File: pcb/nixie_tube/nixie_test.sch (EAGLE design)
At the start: 17 parts, among them IC1 74141N

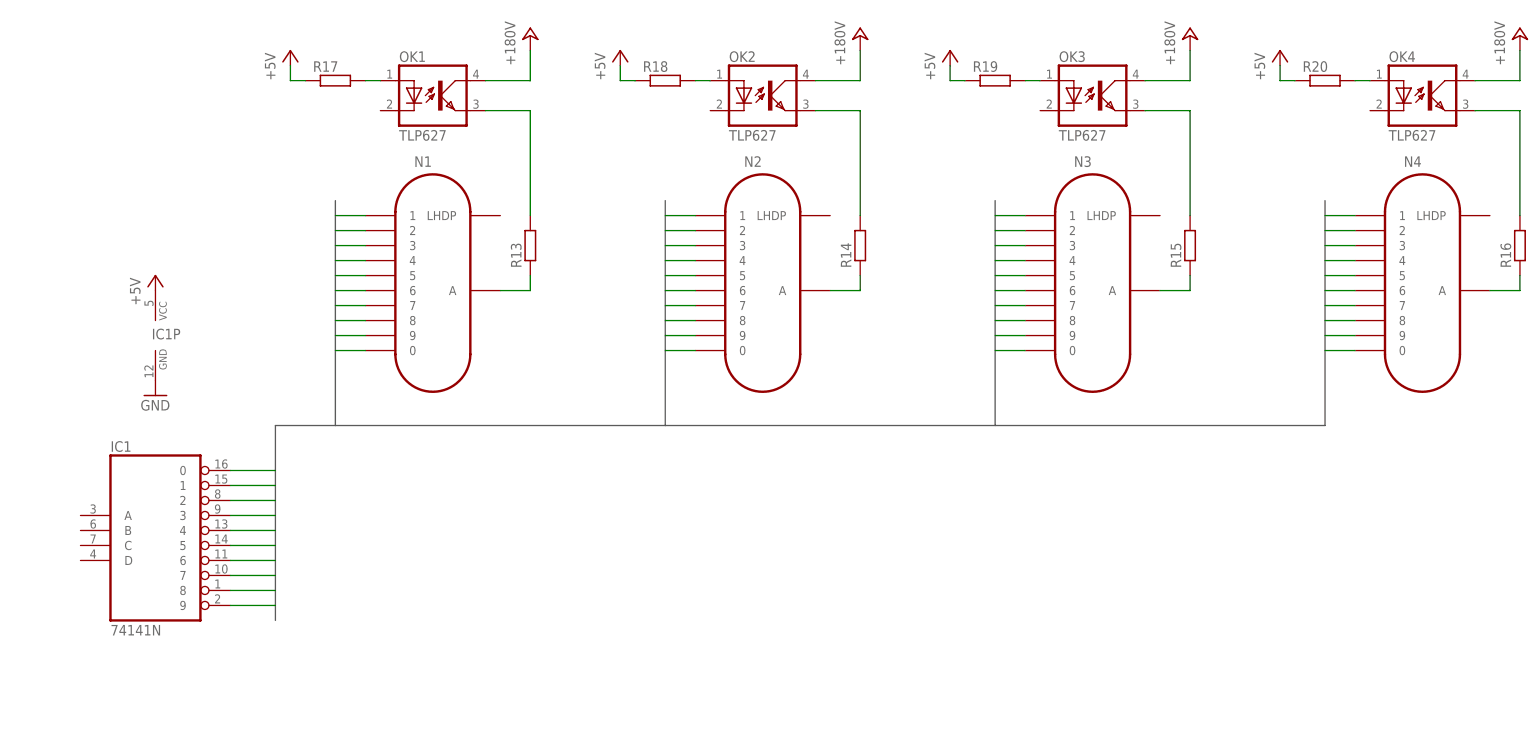
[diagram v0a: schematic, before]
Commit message: 
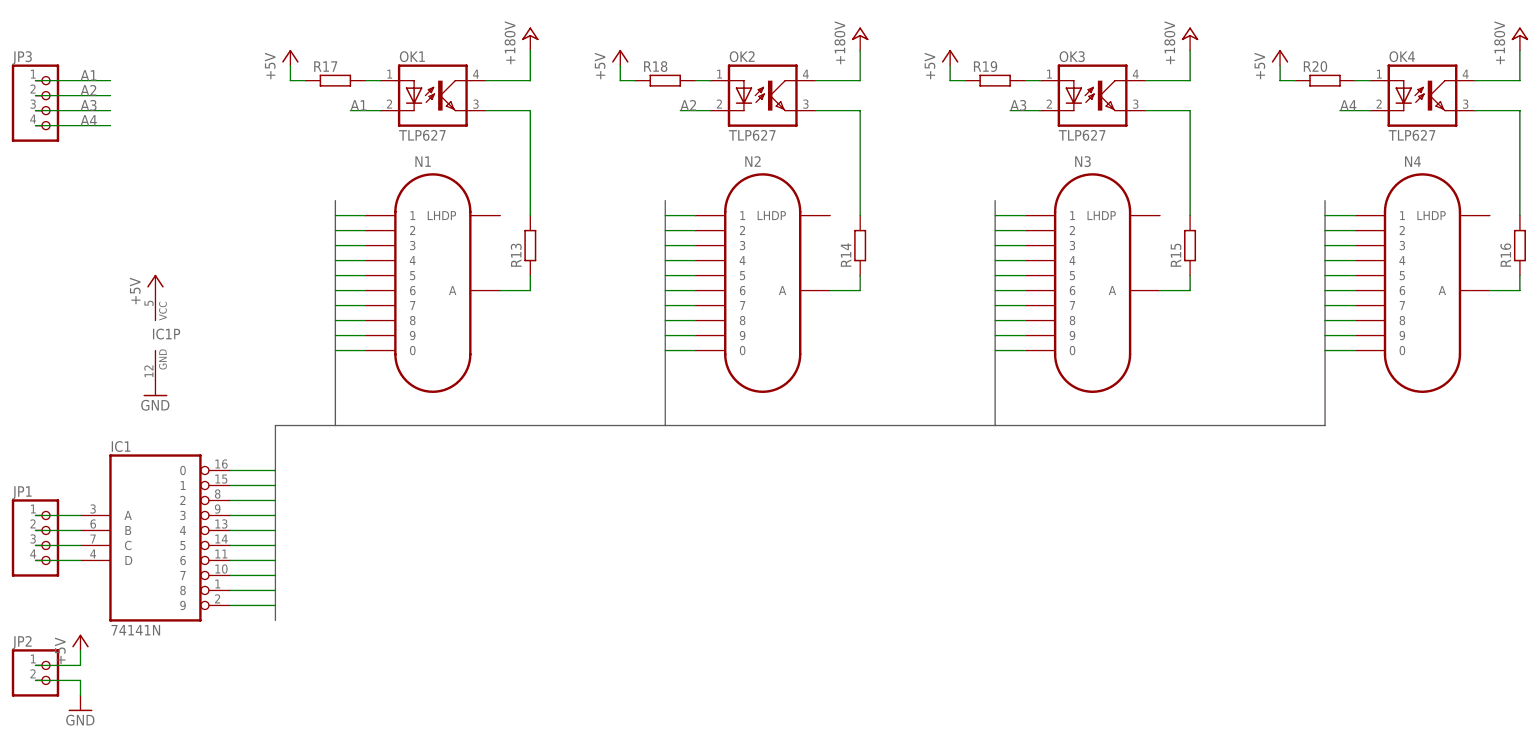
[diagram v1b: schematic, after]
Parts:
- added JP1, JP3: (no value), nixie_tube:PINHD-1X4
- added JP2: (no value), nixie_tube:PINHD-1X2
- R17, R18, R19, R20: device nixie_tube:R-EU_R0805 -> nixie_tube:R-EU_10
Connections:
- new net A1: JP3.1, OK1.C
- new net A2: JP3.2, OK2.C
- new net A3: JP3.3, OK3.C
- new net A4: JP3.4, OK4.C
- new net N$1: IC1A.A, JP1.1
- new net N$2: IC1A.B, JP1.2
- new net N$3: IC1A.C, JP1.3
- new net N$4: IC1A.D, JP1.4
- net +5V: now also JP2.1
- net GND: now also JP2.2
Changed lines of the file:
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@@
 <part name="P+3" library="nixie_tube" deviceset="+180V" device=""/>
 <part name="P+4" library="nixie_tube" deviceset="+180V" device=""/>
-<part name="R17" library="nixie_tube" deviceset="R-EU_" device="R0805"/>
+<part name="R17" library="nixie_tube" deviceset="R-EU_" device="10"/>
 <part name="P+5" library="nixie_tube" deviceset="+5V" device=""/>
-<part name="R18" library="nixie_tube" deviceset="R-EU_" device="R0805"/>
+<part name="R18" library="nixie_tube" deviceset="R-EU_" device="10"/>
 <part name="P+6" library="nixie_tube" deviceset="+5V" device=""/>
-<part name="R19" library="nixie_tube" deviceset="R-EU_" device="R0805"/>
+<part name="R19" library="nixie_tube" deviceset="R-EU_" device="10"/>
 <part name="P+7" library="nixie_tube" deviceset="+5V" device=""/>
-<part name="R20" library="nixie_tube" deviceset="R-EU_" device="R0805"/>
+<part name="R20" library="nixie_tube" deviceset="R-EU_" device="10"/>
 <part name="P+8" library="nixie_tube" deviceset="+5V" device=""/>
 <part name="P+9" library="nixie_tube" deviceset="+5V" device=""/>
 <part name="GND5" library="nixie_tube" deviceset="GND" device=""/>
+<part name="JP1" library="nixie_tube" deviceset="PINHD-1X4" device=""/>
+<part name="JP2" library="nixie_tube" deviceset="PINHD-1X2" device=""/>
+<part name="P+10" library="nixie_tube" deviceset="+5V" device=""/>
+<part name="GND1" library="nixie_tube" deviceset="GND" device=""/>
+<part name="JP3" library="nixie_tube" deviceset="PINHD-1X4" device=""/>
 </parts>
 <sheets>
@@
 <instance part="P+9" gate="1" x="-7.62" y="38.1"/>
 <instance part="GND5" gate="1" x="-7.62" y="17.78"/>
+<instance part="JP1" gate="A" x="-25.4" y="-7.62"/>
+<instance part="JP2" gate="G$1" x="-25.4" y="-30.48"/>
+<instance part="P+10" gate="1" x="-20.32" y="-22.86"/>
+<instance part="GND1" gate="1" x="-20.32" y="-35.56"/>
+<instance part="JP3" gate="A" x="-25.4" y="66.04"/>
 </instances>
 <busses>
@@
 <pinref part="GND5" gate="1" pin="GND"/>
 </segment>
+<segment>
+<pinref part="JP2" gate="G$1" pin="2"/>
+<pinref part="GND1" gate="1" pin="GND"/>
+<wire x1="-27.94" y1="-30.48" x2="-20.32" y2="-30.48" width="0.1524" layer="91"/>
+<wire x1="-20.32" y1="-30.48" x2="-20.32" y2="-33.02" width="0.1524" layer="91"/>
+</segment>
 </net>
 <net name="N$13" class="0">
@@
 <pinref part="P+9" gate="1" pin="+5V"/>
 </segment>
+<segment>
+<pinref part="JP2" gate="G$1" pin="1"/>
+<pinref part="P+10" gate="1" pin="+5V"/>
+<wire x1="-27.94" y1="-27.94" x2="-20.32" y2="-27.94" width="0.1524" layer="91"/>
+<wire x1="-20.32" y1="-27.94" x2="-20.32" y2="-25.4" width="0.1524" layer="91"/>
+</segment>
 </net>
 <net name="N$22" class="0">
@@
 </segment>
 </net>
+<net name="N$1" class="0">
+<segment>
+<pinref part="JP1" gate="A" pin="1"/>
+<pinref part="IC1" gate="A" pin="A"/>
+<wire x1="-27.94" y1="-2.54" x2="-20.32" y2="-2.54" width="0.1524" layer="91"/>
+</segment>
+</net>
+<net name="N$2" class="0">
+<segment>
+<pinref part="JP1" gate="A" pin="2"/>
+<pinref part="IC1" gate="A" pin="B"/>
+<wire x1="-27.94" y1="-5.08" x2="-20.32" y2="-5.08" width="0.1524" layer="91"/>
+</segment>
+</net>
+<net name="N$3" class="0">
+<segment>
+<pinref part="JP1" gate="A" pin="3"/>
+<pinref part="IC1" gate="A" pin="C"/>
+<wire x1="-27.94" y1="-7.62" x2="-20.32" y2="-7.62" width="0.1524" layer="91"/>
+</segment>
+</net>
+<net name="N$4" class="0">
+<segment>
+<pinref part="JP1" gate="A" pin="4"/>
+<pinref part="IC1" gate="A" pin="D"/>
+<wire x1="-27.94" y1="-10.16" x2="-20.32" y2="-10.16" width="0.1524" layer="91"/>
+</segment>
+</net>
+<net name="A1" class="0">
+<segment>
+<pinref part="JP3" gate="A" pin="1"/>
+<wire x1="-27.94" y1="71.12" x2="-15.24" y2="71.12" width="0.1524" layer="91"/>
+<label x="-20.32" y="71.12" size="1.778" layer="95"/>
+</segment>
+<segment>
+<pinref part="OK1" gate="G$1" pin="C"/>
+<wire x1="30.48" y1="66.04" x2="25.4" y2="66.04" width="0.1524" layer="91"/>
+<label x="25.4" y="66.04" size="1.778" layer="95"/>
+</segment>
+</net>
+<net name="A2" class="0">
+<segment>
+<pinref part="JP3" gate="A" pin="2"/>
+<wire x1="-27.94" y1="68.58" x2="-15.24" y2="68.58" width="0.1524" layer="91"/>
+<label x="-20.32" y="68.58" size="1.778" layer="95"/>
+</segment>
+<segment>
+<pinref part="OK2" gate="G$1" pin="C"/>
+<wire x1="86.36" y1="66.04" x2="81.28" y2="66.04" width="0.1524" layer="91"/>
+<label x="81.28" y="66.04" size="1.778" layer="95"/>
+</segment>
+</net>
+<net name="A3" class="0">
+<segment>
+<pinref part="JP3" gate="A" pin="3"/>
+<wire x1="-27.94" y1="66.04" x2="-15.24" y2="66.04" width="0.1524" layer="91"/>
+<label x="-20.32" y="66.04" size="1.778" layer="95"/>
+</segment>
+<segment>
+<pinref part="OK3" gate="G$1" pin="C"/>
+<wire x1="142.24" y1="66.04" x2="137.16" y2="66.04" width="0.1524" layer="91"/>
+<label x="137.16" y="66.04" size="1.778" layer="95"/>
+</segment>
+</net>
+<net name="A4" class="0">
+<segment>
+<pinref part="JP3" gate="A" pin="4"/>
+<wire x1="-27.94" y1="63.5" x2="-15.24" y2="63.5" width="0.1524" layer="91"/>
+<label x="-20.32" y="63.5" size="1.778" layer="95"/>
+</segment>
+<segment>
+<pinref part="OK4" gate="G$1" pin="C"/>
+<wire x1="198.12" y1="66.04" x2="193.04" y2="66.04" width="0.1524" layer="91"/>
+<label x="193.04" y="66.04" size="1.778" layer="95"/>
+</segment>
+</net>
